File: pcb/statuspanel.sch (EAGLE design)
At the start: 8 parts

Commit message: Bump the version number.
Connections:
- net GND: now also DISPLAY.39
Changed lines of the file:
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@@
 <segment>
 <pinref part="DISPLAY" gate="G$1" pin="25"/>
-<wire x1="53.34" y1="68.58" x2="58.42" y2="68.58" width="0.1524" layer="91"/>
+<wire x1="53.34" y1="68.58" x2="55.88" y2="68.58" width="0.1524" layer="91"/>
 <label x="58.42" y="68.58" size="0.8128" layer="95" xref="yes"/>
+<pinref part="DISPLAY" gate="G$1" pin="39"/>
+<wire x1="55.88" y1="68.58" x2="58.42" y2="68.58" width="0.1524" layer="91"/>
+<wire x1="53.34" y1="86.36" x2="55.88" y2="86.36" width="0.1524" layer="91"/>
+<wire x1="55.88" y1="86.36" x2="55.88" y2="68.58" width="0.1524" layer="91"/>
 </segment>
 </net>

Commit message: Change the busy pin.
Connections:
- net BUSY: now also HUZZAH32.GPIOSCL; no longer HUZZAH32.GPIO13
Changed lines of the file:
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@@
 </segment>
 <segment>
-<pinref part="HUZZAH32" gate="G$1" pin="GPIO13"/>
-<wire x1="91.44" y1="66.04" x2="86.36" y2="66.04" width="0.1524" layer="91"/>
-<label x="86.36" y="66.04" size="0.8128" layer="95" rot="R180" xref="yes"/>
+<pinref part="HUZZAH32" gate="G$1" pin="GPIOSCL"/>
+<wire x1="91.44" y1="83.82" x2="86.36" y2="83.82" width="0.1524" layer="91"/>
+<label x="86.36" y="83.82" size="0.8128" layer="95" rot="R180" xref="yes"/>
 </segment>
 </net>

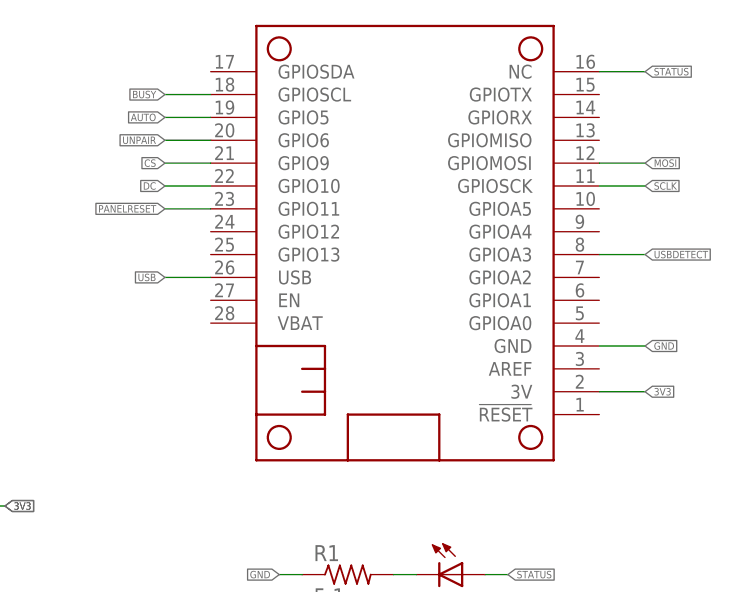
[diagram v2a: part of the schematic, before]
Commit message: This corrects the pin names on the huzzah32 but makes no other changes.
Adds a new eagle library tomscis_huzzah32.lbr with the updated
component in. Note even though I removed the through holes from the
FEATHERWING_NODIM footprint, they still appear on the statuspanel
board layout. I can remove them there too if desired?
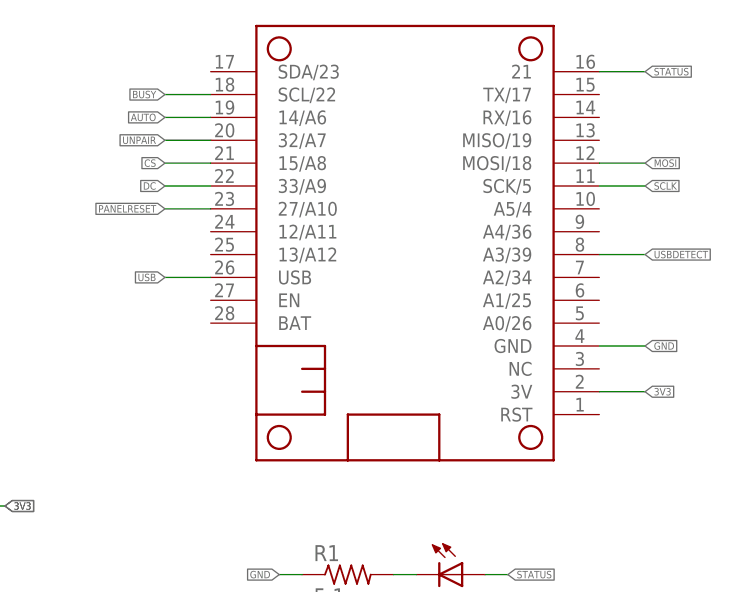
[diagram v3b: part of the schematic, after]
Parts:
- HUZZAH32: value FEATHERWING_NODIM -> HUZZAH32_NODIM; device adafruit:FEATHERWING_NODIM -> tomscis_huzzah32:HUZZAH32_NODIM
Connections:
- net AUTO: now also HUZZAH32.14/A6; no longer HUZZAH32.GPIO5
- net BUSY: now also HUZZAH32.SCL/22; no longer HUZZAH32.GPIOSCL
- net CS: now also HUZZAH32.15/A8; no longer HUZZAH32.GPIO9
- net DC: now also HUZZAH32.33/A9; no longer HUZZAH32.GPIO10
- net MOSI: now also HUZZAH32.MOSI/18; no longer HUZZAH32.GPIOMOSI
- net PANELRESET: now also HUZZAH32.27/A10; no longer HUZZAH32.GPIO11
- net SCLK: now also HUZZAH32.SCK/5; no longer HUZZAH32.GPIOSCK
- net STATUS: now also HUZZAH32.21; no longer HUZZAH32.NC
- net UNPAIR: now also HUZZAH32.32/A7; no longer HUZZAH32.GPIO6
- net USBDETECT: now also HUZZAH32.A3/39; no longer HUZZAH32.GPIOA3
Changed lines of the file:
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@@
 <layer number="1" name="Top" color="4" fill="1" visible="no" active="no"/>
 <layer number="2" name="Route2" color="1" fill="3" visible="no" active="no"/>
+<layer number="3" name="Route3" color="4" fill="3" visible="no" active="no"/>
+<layer number="4" name="Route4" color="1" fill="4" visible="no" active="no"/>
+<layer number="5" name="Route5" color="4" fill="4" visible="no" active="no"/>
+<layer number="6" name="Route6" color="1" fill="8" visible="no" active="no"/>
+<layer number="7" name="Route7" color="4" fill="8" visible="no" active="no"/>
+<layer number="8" name="Route8" color="1" fill="2" visible="no" active="no"/>
+<layer number="9" name="Route9" color="4" fill="2" visible="no" active="no"/>
+<layer number="10" name="Route10" color="1" fill="7" visible="no" active="no"/>
+<layer number="11" name="Route11" color="4" fill="7" visible="no" active="no"/>
+<layer number="12" name="Route12" color="1" fill="5" visible="no" active="no"/>
+<layer number="13" name="Route13" color="4" fill="5" visible="no" active="no"/>
+<layer number="14" name="Route14" color="1" fill="6" visible="no" active="no"/>
 <layer number="15" name="Route15" color="4" fill="6" visible="no" active="no"/>
 <layer number="16" name="Bottom" color="1" fill="1" visible="no" active="no"/>
@@
 </classes>
 <parts>
-<part name="HUZZAH32" library="adafruit" library_urn="urn:adsk.eagle:library:420" deviceset="FEATHERWING" device="_NODIM"/>
+<part name="HUZZAH32" library="tomscis_huzzah32" deviceset="HUZZAH32" device="_NODIM"/>
 <part name="DISPLAY" library="con-lstb" library_urn="urn:adsk.eagle:library:162" deviceset="MA20-2" device="" package3d_urn="urn:adsk.eagle:package:8338/1"/>
 <part name="AUTO" library="adafruit" library_urn="urn:adsk.eagle:library:420" deviceset="EG1218" device="S" package3d_urn="urn:adsk.eagle:package:6240649/1"/>
@@
 </segment>
 <segment>
-<pinref part="HUZZAH32" gate="G$1" pin="GPIO11"/>
+<pinref part="HUZZAH32" gate="G$1" pin="27/A10"/>
 <wire x1="91.44" y1="71.12" x2="86.36" y2="71.12" width="0.1524" layer="91"/>
 <label x="86.36" y="71.12" size="0.8128" layer="95" rot="R180" xref="yes"/>
@@
 </segment>
 <segment>
-<pinref part="HUZZAH32" gate="G$1" pin="GPIOMOSI"/>
+<pinref part="HUZZAH32" gate="G$1" pin="MOSI/18"/>
 <wire x1="134.62" y1="76.2" x2="139.7" y2="76.2" width="0.1524" layer="91"/>
 <label x="139.7" y="76.2" size="0.8128" layer="95" xref="yes"/>
@@
 </segment>
 <segment>
-<pinref part="HUZZAH32" gate="G$1" pin="GPIOSCK"/>
+<pinref part="HUZZAH32" gate="G$1" pin="SCK/5"/>
 <wire x1="134.62" y1="73.66" x2="139.7" y2="73.66" width="0.1524" layer="91"/>
 <label x="139.7" y="73.66" size="0.8128" layer="95" xref="yes"/>
@@
 </segment>
 <segment>
-<pinref part="HUZZAH32" gate="G$1" pin="GPIO9"/>
+<pinref part="HUZZAH32" gate="G$1" pin="15/A8"/>
 <wire x1="91.44" y1="76.2" x2="86.36" y2="76.2" width="0.1524" layer="91"/>
 <label x="86.36" y="76.2" size="0.8128" layer="95" rot="R180" xref="yes"/>
@@
 </segment>
 <segment>
-<pinref part="HUZZAH32" gate="G$1" pin="GPIO10"/>
+<pinref part="HUZZAH32" gate="G$1" pin="33/A9"/>
 <wire x1="91.44" y1="73.66" x2="86.36" y2="73.66" width="0.1524" layer="91"/>
 <label x="86.36" y="73.66" size="0.8128" layer="95" rot="R180" xref="yes"/>
@@
 </segment>
 <segment>
-<pinref part="HUZZAH32" gate="G$1" pin="GPIOSCL"/>
+<pinref part="HUZZAH32" gate="G$1" pin="SCL/22"/>
 <wire x1="91.44" y1="83.82" x2="86.36" y2="83.82" width="0.1524" layer="91"/>
 <label x="86.36" y="83.82" size="0.8128" layer="95" rot="R180" xref="yes"/>
@@
 <net name="AUTO" class="0">
 <segment>
-<pinref part="HUZZAH32" gate="G$1" pin="GPIO5"/>
+<pinref part="HUZZAH32" gate="G$1" pin="14/A6"/>
 <wire x1="91.44" y1="81.28" x2="86.36" y2="81.28" width="0.1524" layer="91"/>
 <label x="86.36" y="81.28" size="0.8128" layer="95" rot="R180" xref="yes"/>
@@
 </segment>
 <segment>
-<pinref part="HUZZAH32" gate="G$1" pin="GPIO6"/>
+<pinref part="HUZZAH32" gate="G$1" pin="32/A7"/>
 <wire x1="91.44" y1="78.74" x2="86.36" y2="78.74" width="0.1524" layer="91"/>
 <label x="86.36" y="78.74" size="0.8128" layer="95" rot="R180" xref="yes"/>
@@
 </segment>
 <segment>
-<pinref part="HUZZAH32" gate="G$1" pin="NC"/>
+<pinref part="HUZZAH32" gate="G$1" pin="21"/>
 <wire x1="134.62" y1="86.36" x2="139.7" y2="86.36" width="0.1524" layer="91"/>
 <label x="139.7" y="86.36" size="0.8128" layer="95" xref="yes"/>
@@
 <net name="USBDETECT" class="0">
 <segment>
-<pinref part="HUZZAH32" gate="G$1" pin="GPIOA3"/>
+<pinref part="HUZZAH32" gate="G$1" pin="A3/39"/>
 <wire x1="134.62" y1="66.04" x2="139.7" y2="66.04" width="0.1524" layer="91"/>
 <label x="139.7" y="66.04" size="0.8128" layer="95" xref="yes"/>
